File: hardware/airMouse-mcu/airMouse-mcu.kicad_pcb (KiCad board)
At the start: 2 copper layers, 56.5 x 64.5 mm, 115 parts, among them J1 MCU_PRG, J2 RADIO_PRG, J3 AT, J4 DS1020-07-16VBT1A-R, J5 DS1020-07-10VBT1A-R, J6 Conn_01x04_MountingPin, Q1 IRLML6346, SW1 KEY, U1 LSM6DS3, U2 MCP1640CT-I/CHY, U3 STM32G071RBTx, U4 ESP32-C3-WROOM-02U

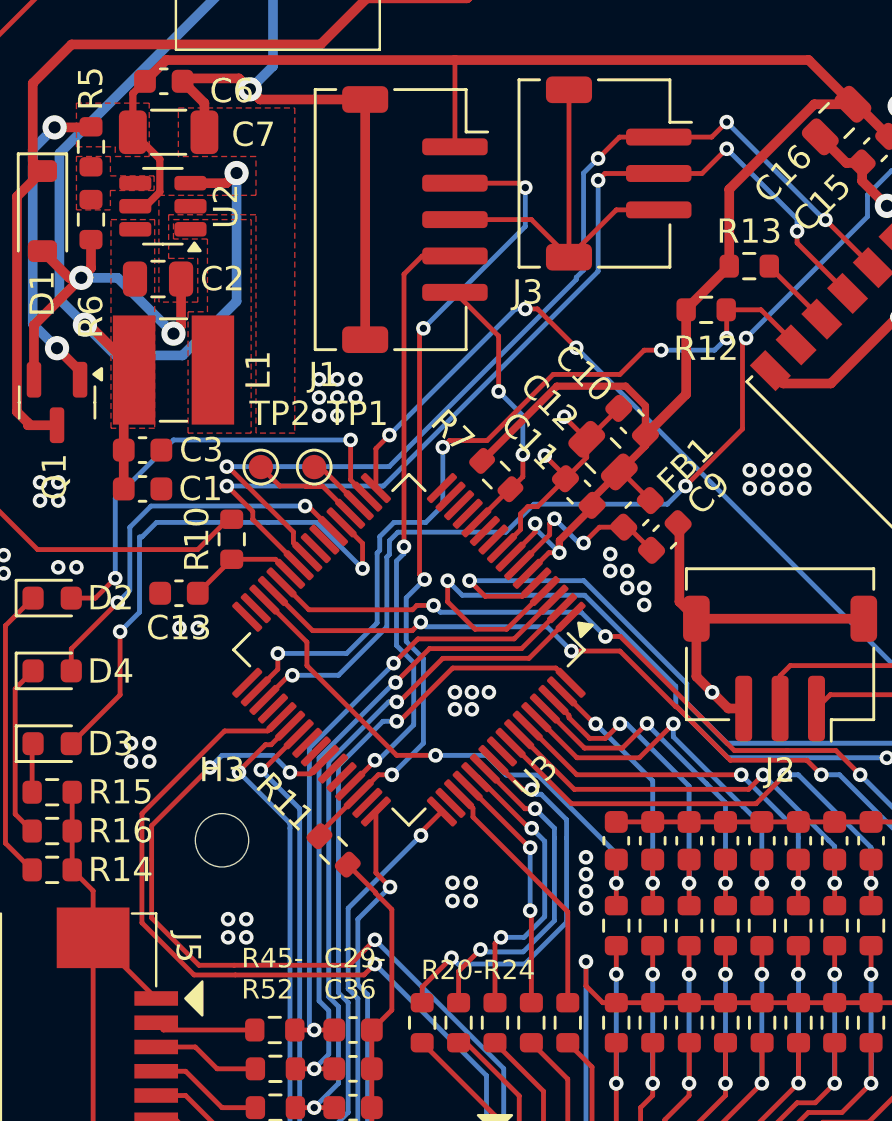
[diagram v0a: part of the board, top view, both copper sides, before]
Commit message: add connectors 3d models
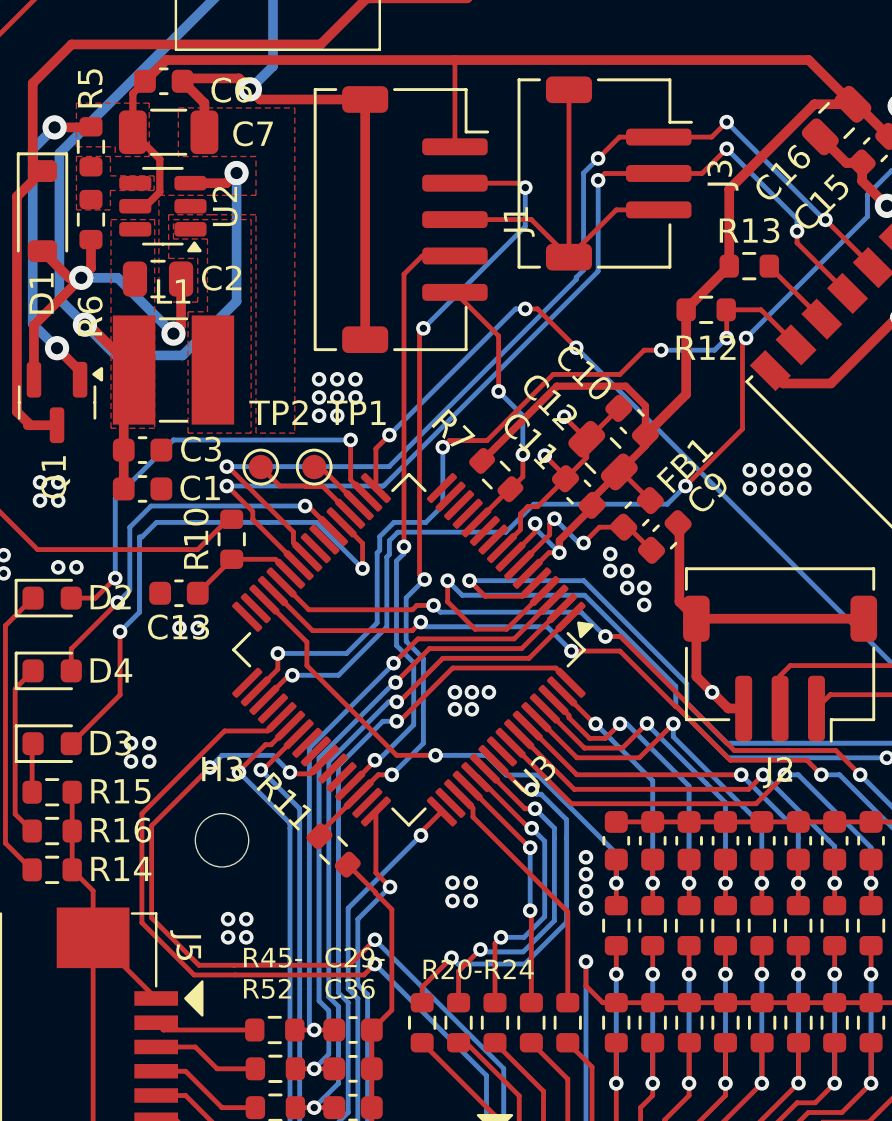
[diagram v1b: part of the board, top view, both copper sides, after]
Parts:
- C1: value 105 -> 1u
- J1: footprint Connector_JST:JST_ZH_S5B-ZR-SM4A-TF_1x05-1MP_P1.50mm_Horizontal -> airMouseLib:JST_ZH_S5B-ZR-SM4A-TF_1x05-1MP_P1.50mm_Horizontal
- J2, J3: footprint Connector_JST:JST_ZH_S3B-ZR-SM4A-TF_1x03-1MP_P1.50mm_Horizontal -> airMouseLib:JST_ZH_S3B-ZR-SM4A-TF_1x03-1MP_P1.50mm_Horizontal
- J6: value Conn_01x04_MountingPin -> DS1020-07-4VBT1A-R
- L1: footprint Inductor_SMD:L_Ferrocore_DLG-0403 -> airMouseLib:L_Ferrocore_DLG-0403
- U1: value LSM6DS3 -> LSM6DS3TR-C
